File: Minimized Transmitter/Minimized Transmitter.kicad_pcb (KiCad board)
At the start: 2 copper layers, 27.1 x 27.1 mm, 11 parts, among them J1 Conn_01x03_Male, J2 Conn_01x02_Male, J4 Conn_01x05_Male, SW1 SW_Push, U1 LPC824M201JHI33, U2 RFM69HCW

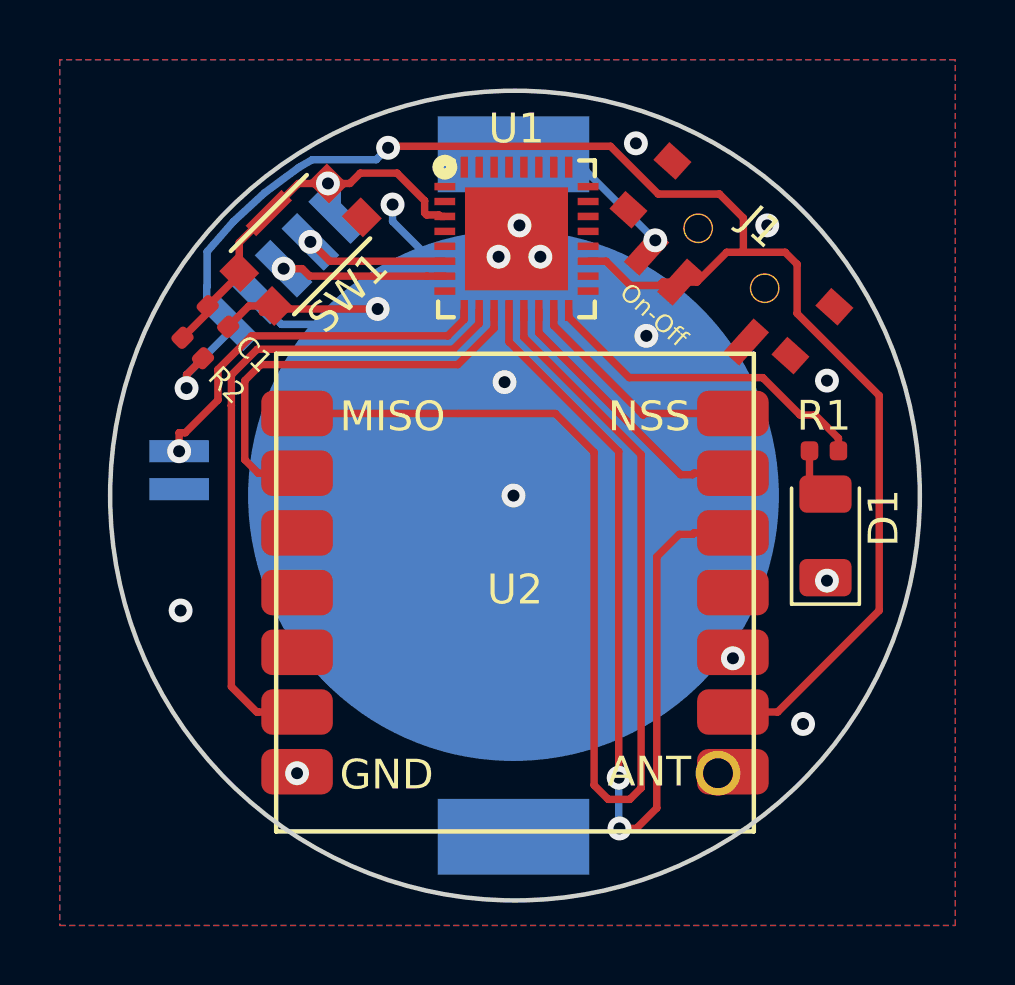
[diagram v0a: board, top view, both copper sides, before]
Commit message: Added Copper planes around the Batery holder to make the pads more secure on the board.
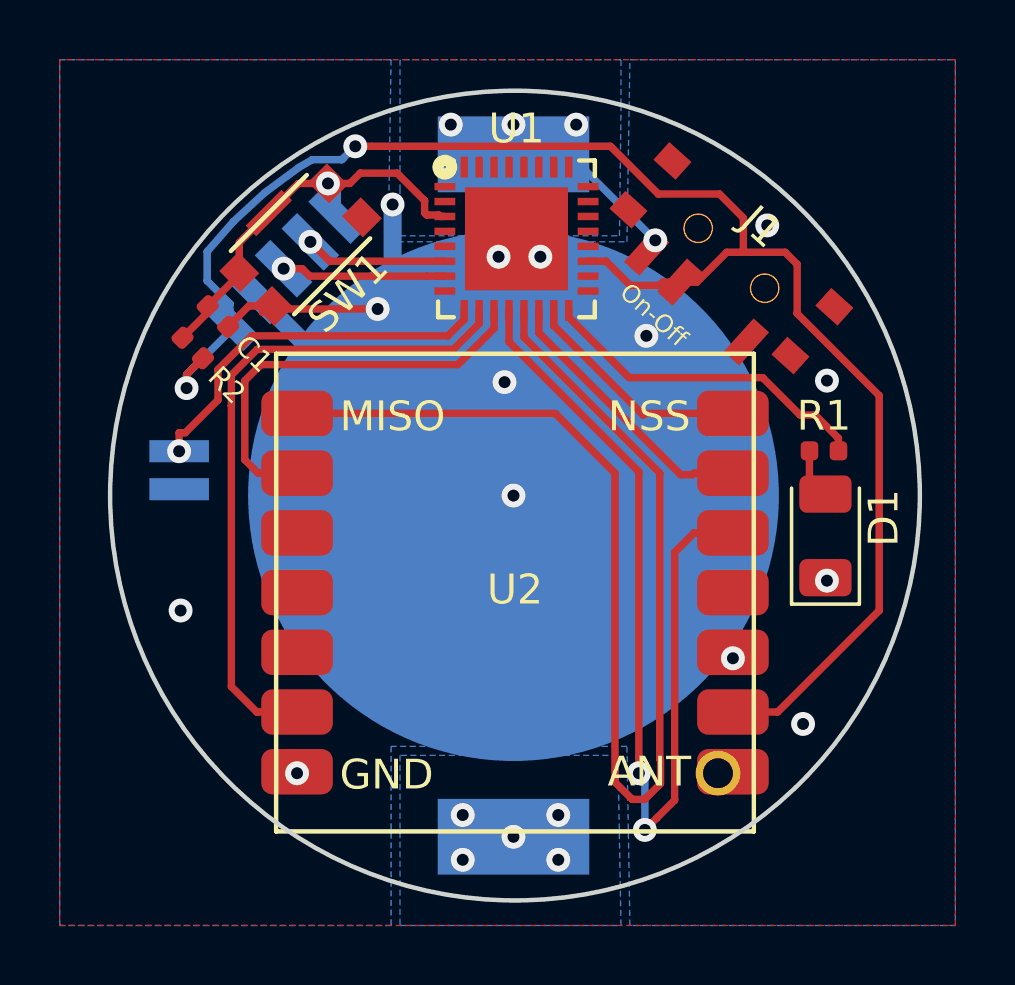
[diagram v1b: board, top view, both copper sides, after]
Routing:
- net GND: track 28.5 -> 28.4 mm, vias 16 -> 14
- net Net-(BT1-Pad1): vias 1 -> 9
- added copper zone on B.Cu, net Net-(BT1-Pad1)
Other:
- board text added: "V1.1"
